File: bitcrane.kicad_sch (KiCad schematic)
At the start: 130 parts, among them J1 PSU Comm, J12 0455580003, J13 Hashboard0, J13 Hashboard1, J13 Hashboard2, J14 0353180420, J15 0353180420, J16 0353180420, J17 0353180420, J3 61900411021, J4 61900411021, J8 USB_C_Receptacle_USB2.0, Q1 DMP3013SFV-7, U1 FT4232HQ, U10 PCA9546ARGVR, U2 RT9080-33GJ5, U3 M93C46-WDW6TP, U5 EMC2305, Y1 12MHz

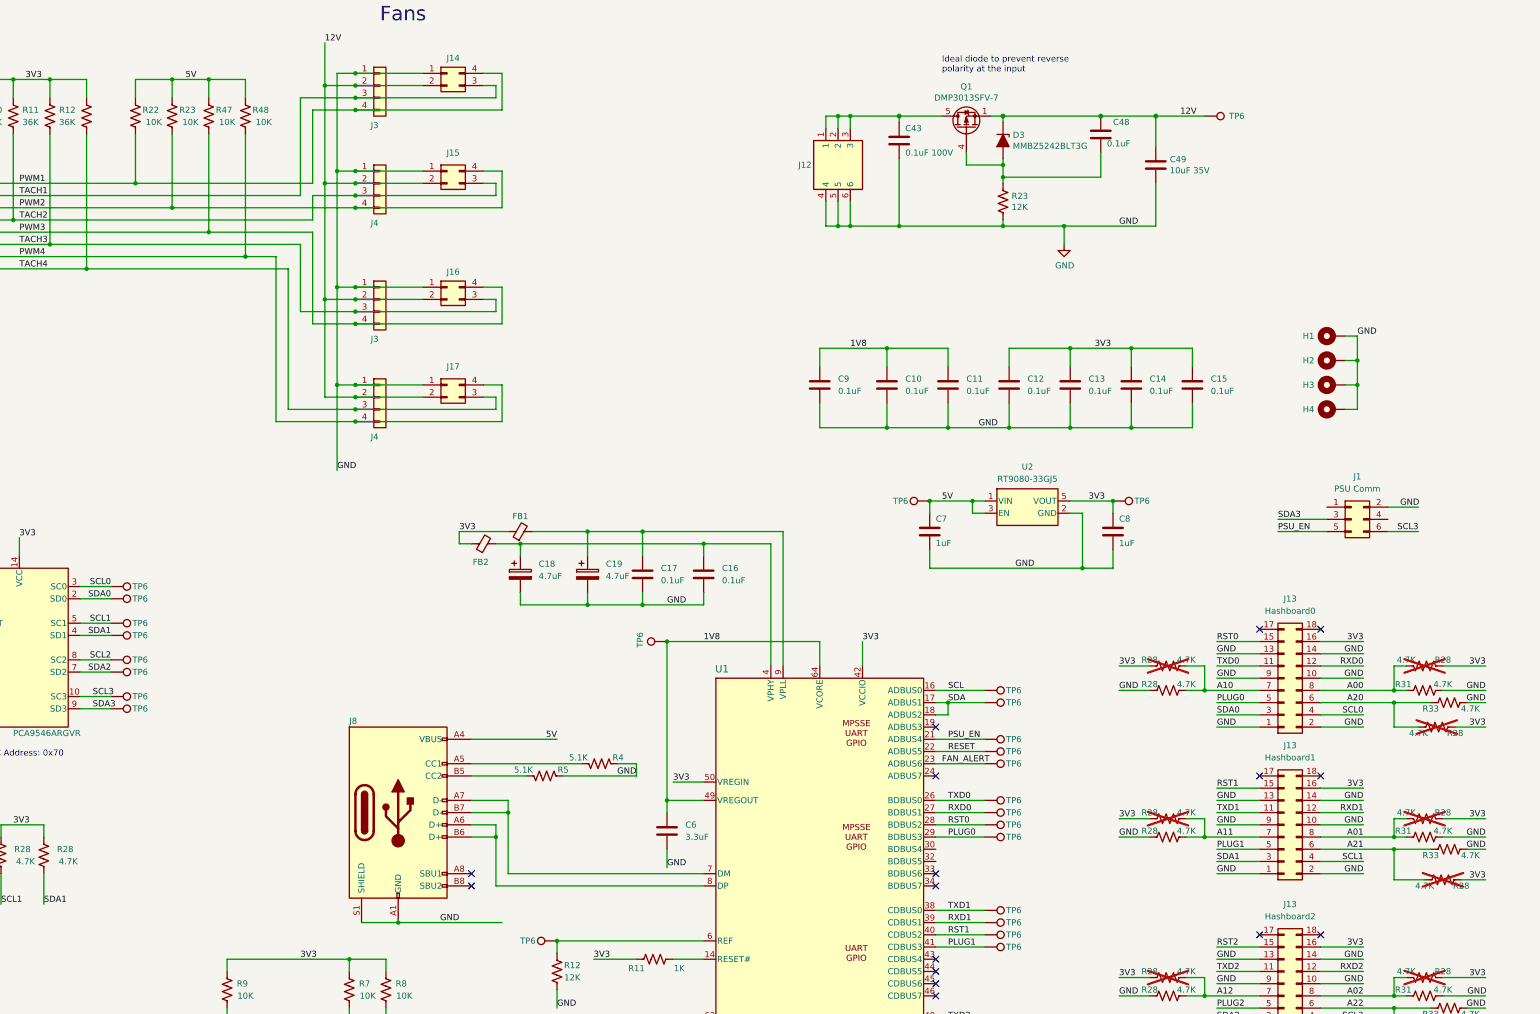
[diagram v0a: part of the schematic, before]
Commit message: added PCB labels for Fans and Hashboards. Starting to add LCSC part numbers
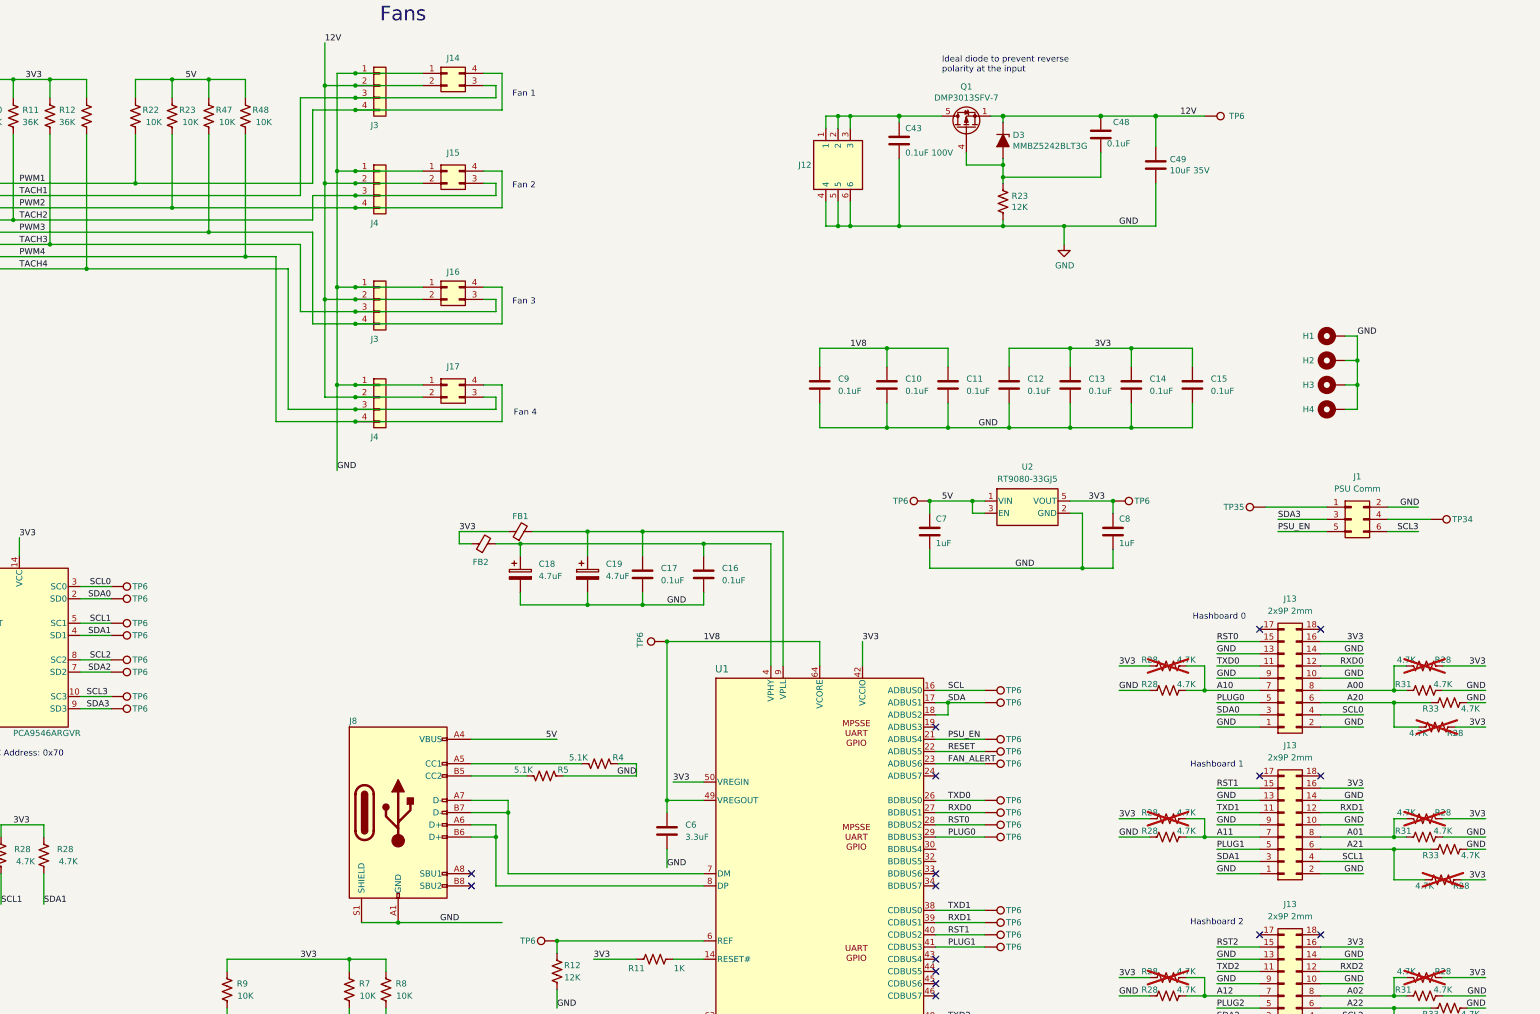
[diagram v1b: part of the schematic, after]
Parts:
- added TP34, TP35: TestPoint, TestPoint:TestPoint_Pad_D1.5mm, symbol Connector:TestPoint
- J12: JLCPCB (none) -> C492365; LCSC (none) -> C492365
- J13: value Hashboard0 -> 2x9P 2mm; JLCPCB (none) -> C437089
- J13: value Hashboard1 -> 2x9P 2mm; JLCPCB (none) -> C437089
- J13: value Hashboard2 -> 2x9P 2mm; JLCPCB (none) -> C437089
- J14, J15, J16, J17: JLCPCB (none) -> C54909; LCSC (none) -> C54909
- J8: JLCPCB (none) -> C2988369; LCSC (none) -> C2988369
- Q1: JLCPCB (none) -> C264098; LCSC (none) -> C264098
- U1: JLCPCB (none) -> C2651882
- U2: JLCPCB (none) -> C841192
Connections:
- net at J1.1 (Pin_1): now also TP35.1
- net at J1.4 (Pin_4): now also TP34.1
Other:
- note added: "Fan 1"
- note added: "Fan 2"
- note added: "Fan 3"
- note added: "Fan 4"
- note added: "Hashboard 0"
- note added: "Hashboard 1"
- note added: "Hashboard 2"

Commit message: added almost all LCSC part numbers
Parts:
- removed C17: 0.1uF, Capacitor_SMD:C_0805_2012Metric, symbol Device:C
- removed C18, C19: 4.7uF, Capacitor_SMD:CP_Elec_4x5.4, symbol Device:C_Polarized
- removed R28 (x8): 4.7K, Resistor_SMD:R_0805_2012Metric, symbol Device:R_US
- removed TP6 (x9): TestPoint, TestPoint:TestPoint_Pad_D1.5mm, symbol Connector:TestPoint
- removed U10: PCA9546ARGVR, bitcart:QFN-16_EP_4x4_Pitch0.65mm, symbol bitcart:PCA9546ARGVR
- added C18, C21: 47uF, Capacitor_SMD:C_0805_2012Metric, symbol Device:C
- C1, C2: DK 1276-2622-1-ND -> (none); LCSC (none) -> C107113; PARTNO CL21C270JCANNNC -> CC0805JRNPO9BN270
- C10, C11, C12, C13, C14, C15, C16, C17, C48, C9: LCSC (none) -> C28233
- C43: value 0.1uF 100V -> 0.1uF; LCSC (none) -> C28233
- C49: LCSC (none) -> C440198
- C6: LCSC (none) -> C159781
- C7, C8: LCSC (none) -> C116352
- D3: value MMBZ5242BLT3G -> LBZX84C12LT1G; DK MMBZ5242BLT3GOSCT-ND -> (none); LCSC (none) -> C12773; PARTNO MMBZ5242BLT3G -> LBZX84C12LT1G
- FB1, FB2: LCSC (none) -> C19330
- J1: LCSC (none) -> C2845614
- J12: JLCPCB C492365 -> (none)
- J13: JLCPCB C437089 -> (none)
- J14, J15, J16, J17: JLCPCB C54909 -> (none)
- J3, J4: LCSC (none) -> C2982043
- J8: JLCPCB C2988369 -> (none)
- Q1: JLCPCB C264098 -> (none)
- R10, R11, R12, R9: value 36K -> 36k; LCSC (none) -> C114527
- R11: value 1K -> 1k; LCSC (none) -> C95781
- R12, R23: value 12K -> 12k; LCSC (none) -> C114556
- R17: LCSC (none) -> C869381
- R18: LCSC (none) -> C114565
- R19: LCSC (none) -> C60816
- R22, R23, R47, R48, R7, R8, R9: value 10K -> 10k; LCSC (none) -> C84376
- R28: value 4.7K -> 4.7k; LCSC (none) -> C60816; now left out of the parts list
- R28, R31, R33: value 4.7K -> 4.7k; LCSC (none) -> C60816
- R28: value 4.7K -> 4.7k; LCSC (none) -> C60816; now fitted
- R28, R31: value 4.7K -> 4.7k; LCSC (none) -> C60816; now not fitted; now left out of the parts list
- R4, R5: value 5.1K -> 5.1k; LCSC (none) -> C84375
- R6: value 2.2K -> 2.2k; LCSC (none) -> C114561
- U1: JLCPCB C2651882 -> (none); LCSC (none) -> C2651882
- U2: JLCPCB C841192 -> (none); LCSC (none) -> C841192
- U3: LCSC (none) -> C616741
- Y1: footprint bitcrane:XTAL_405C35B12M00000 -> Crystal:Crystal_SMD_3225-4Pin_3.2x2.5mm; DK CTX639CT-ND -> (none); LCSC (none) -> C21900467; PARTNO 405C35B12M00000 -> (none)
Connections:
- net SCL0 is gone; now on net SCL: J13.4 (Pin_4)
- net SCL1 is gone; now on net SCL: J13.4 (Pin_4)
- net SCL2 is gone; now on net SCL: J13.4 (Pin_4)
- net SCL3 is gone; now on net SCL: J1.6 (Pin_6), U5.2 (SMCLK)
- net SDA0 is gone; now on net SDA: J13.3 (Pin_3)
- net SDA1 is gone; now on net SDA: J13.3 (Pin_3)
- net SDA2 is gone; now on net SDA: J13.3 (Pin_3)
- net SDA3 is gone; now on net SDA: J1.3 (Pin_3), U5.1 (SMDATA)
- net GND: now also C18.2, C21.2
- net at C16.1, FB2.2, U1.4 (VPHY): now also C18.1
- net at C17.1, FB1.2, U1.9 (VPLL): now also C21.1
- net RESET: no longer names the net of U1.22 (ADBUS5)
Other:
- note removed: "I2C Address: 0x70"
- moved on the sheet: C1, C16, C17, C2, C6, FB1, FB2, J8, R11, R12, R4, R5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

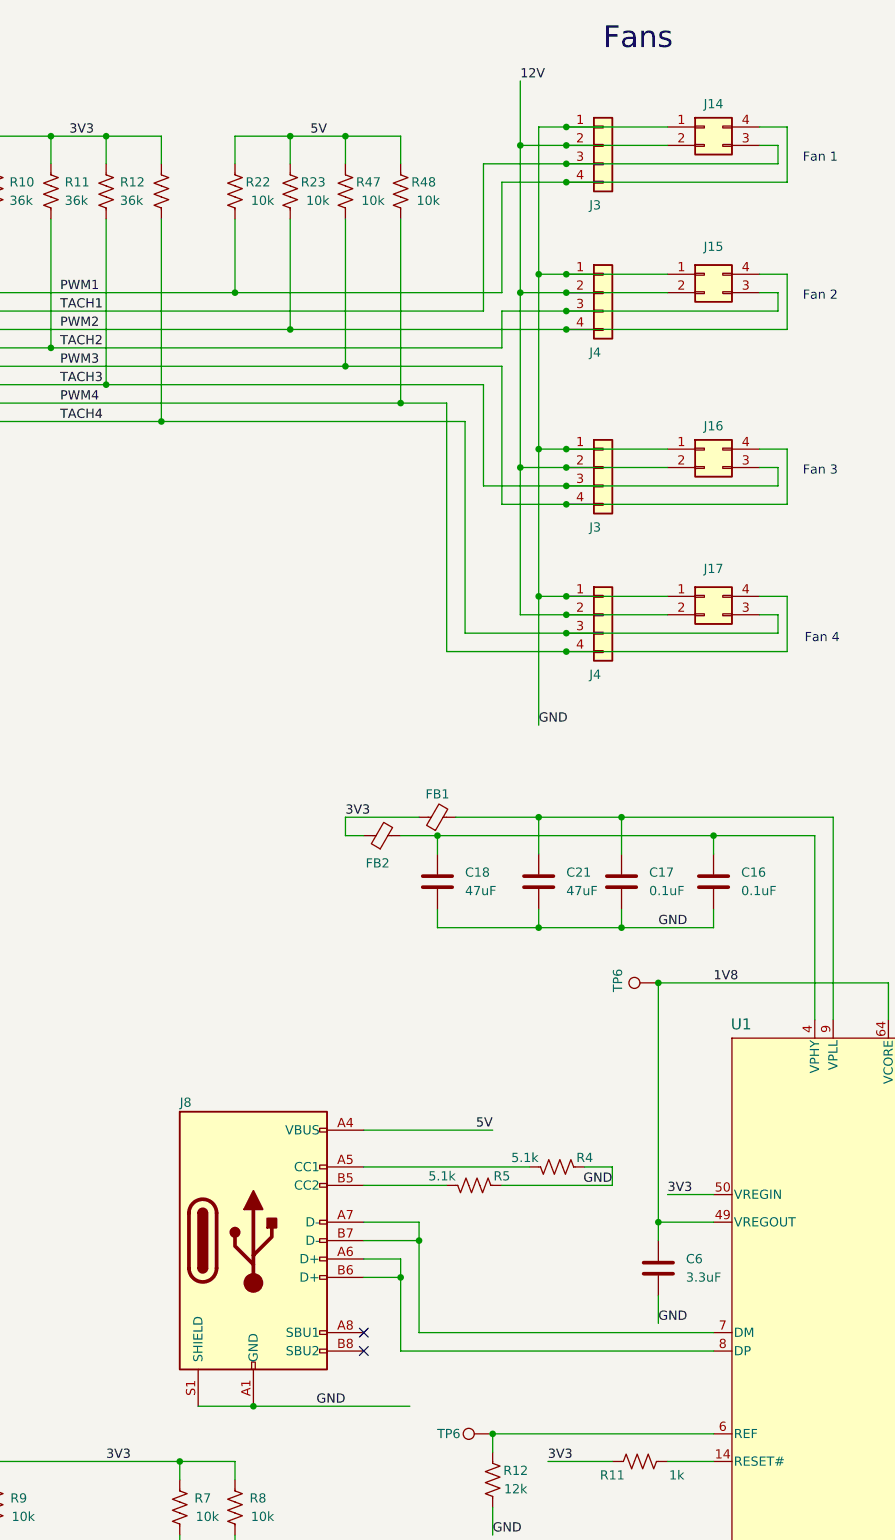
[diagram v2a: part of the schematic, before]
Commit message: Updated all footprints for JLCPCB parts. Added JLCPCB BOM and CPL
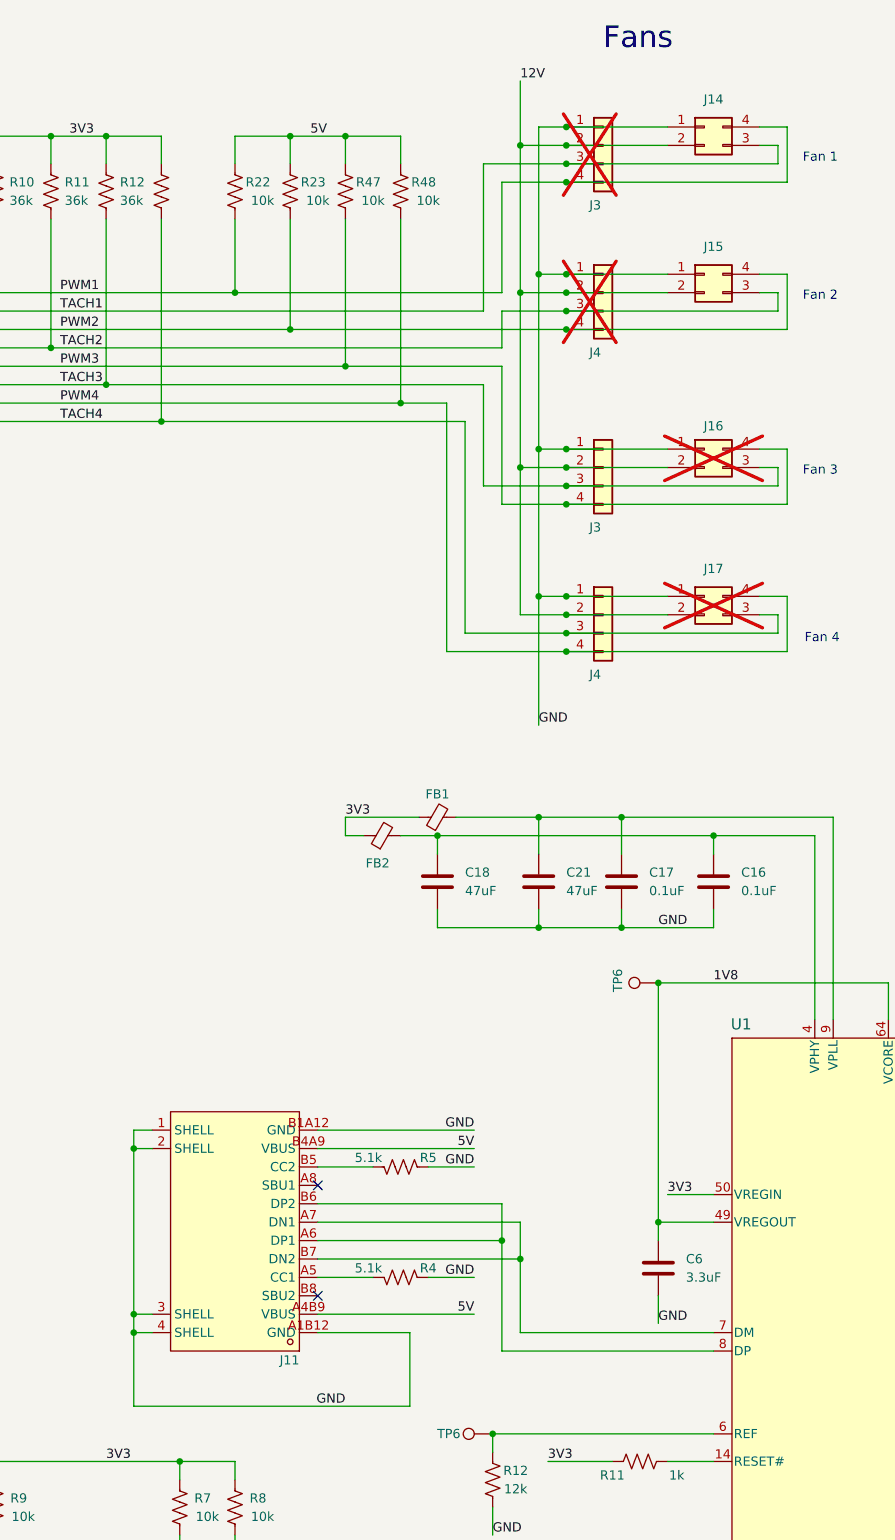
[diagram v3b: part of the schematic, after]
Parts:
- removed J8: USB_C_Receptacle_USB2.0, Connector_USB:USB_C_Receptacle_GCT_USB4105-xx-A_16P_TopMnt_Horizontal, symbol Connector:USB_C_Receptacle_USB2.0
- added J11: USB_C_Receptacle_USB2.0, bitcrane:USB-C-SMD_G-SWITCH_GT-USB-7010ASV, symbol bitcrane:GT-USB-7010ASV
- C7, C8: LCSC C116352 -> C28323
- D3: footprint bitcart:D_SOT-23_ANK -> bitcrane:SOT-23-3_L2.9-W1.6-P1.90-LS2.8-BR
- J12: footprint bitcart:0455580003 -> bitcrane:CONN-TH_50362462
- J14, J15: footprint bitcrane:MOLEX_353180420 -> bitcrane:CONN-TH_4P-P4.20_5557-2X2AW
- J16, J17: footprint bitcrane:MOLEX_353180420 -> bitcrane:CONN-TH_4P-P4.20_5557-2X2AW; now not fitted; now left out of the parts list
- J3, J4: footprint bitcart:CONN_61900411021_WRE -> bitcrane:CONN-TH_4P-P2.54_HCTL_HC-2510-4AW; now not fitted; now left out of the parts list
- J3, J4: footprint bitcart:CONN_61900411021_WRE -> bitcrane:CONN-TH_4P-P2.54_HCTL_HC-2510-4AW
- Q1: footprint Package_SON:Diodes_PowerDI3333-8 -> bitcrane:POWERPAK-1212-8_L3.1-W3.1-P0.65-LS3.3-BL; symbol Transistor_FET:DMP3013SFV -> bitcrane:DMP3013SFV
- R11: LCSC C95781 -> C17513
- R12, R23: LCSC C114556 -> C17444
- R17: LCSC C869381 -> C17633
- R18: LCSC C114565 -> C17560
- R19, R28, R31, R33: LCSC C60816 -> C17673
- R22, R23, R47, R48, R7, R8, R9: LCSC C84376 -> C17414
- R4, R5: LCSC C84375 -> C27834
- R6: LCSC C114561 -> C17520
- U2: footprint bitaxe:RT9080-33GJ5 -> bitcrane:TSOT-23-5_L2.9-W1.6-P0.95-LS2.8-BL
- U3: footprint bitcrane:TSSOP8_STM -> bitcrane:TSSOP-8_L4.4-W3.0-P0.65-LS6.4-BL
- Y1: LCSC C21900467 -> C251626
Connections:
- net 5V: now also J11.A4B9 (VBUS), J11.B4A9 (VBUS)
- net GND: now also J11.1 (SHELL), J11.2 (SHELL), J11.3 (SHELL), J11.4 (SHELL), J11.A1B12 (GND), J11.B1A12 (GND)
- net at U1.7 (DM): now also J11.A7 (DN1), J11.B7 (DN2)
- net at U1.8 (DP): now also J11.A6 (DP1), J11.B6 (DP2)
- net at C43.1, J12.1, J12.2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: now also Q1.6 (D), Q1.7 (D), Q1.8 (D)
- net at R4.2: now also J11.A5 (CC1)
- net at R5.2: now also J11.B5 (CC2)
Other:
- moved on the sheet: R4, R5

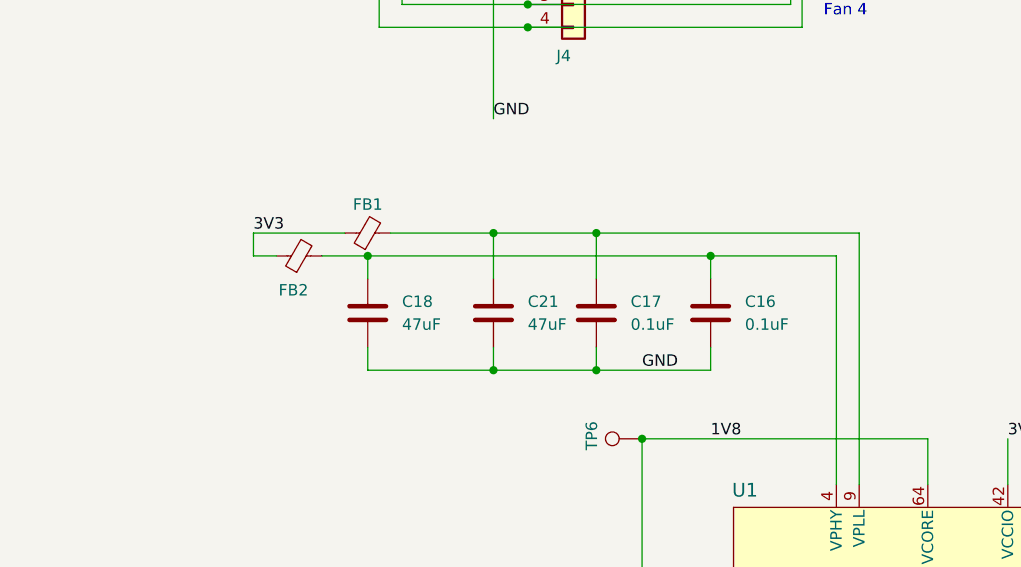
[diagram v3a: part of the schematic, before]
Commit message: changed Y1 LCSC partnumber for #12 Changed C18/C21 value in schematic (thanks @BeeEvolved)
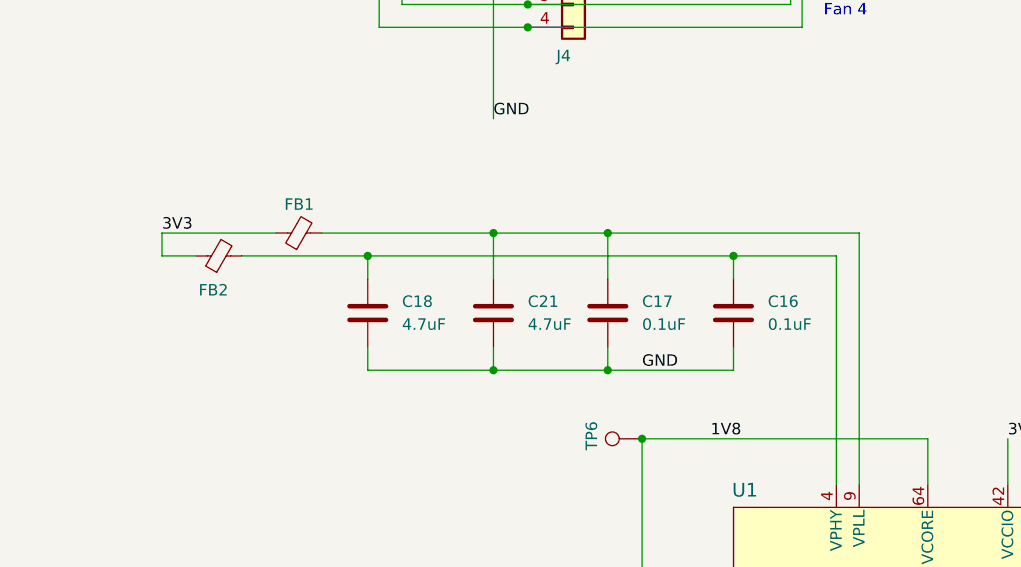
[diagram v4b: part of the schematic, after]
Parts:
- C18, C21: value 47uF -> 4.7uF
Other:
- moved on the sheet: C16, C17, FB1, FB2
